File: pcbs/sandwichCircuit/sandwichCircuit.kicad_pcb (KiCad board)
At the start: 2 copper layers, 2 parts, among them J1 Conn_01x19_Pin, U1 ESP32-DevKitC

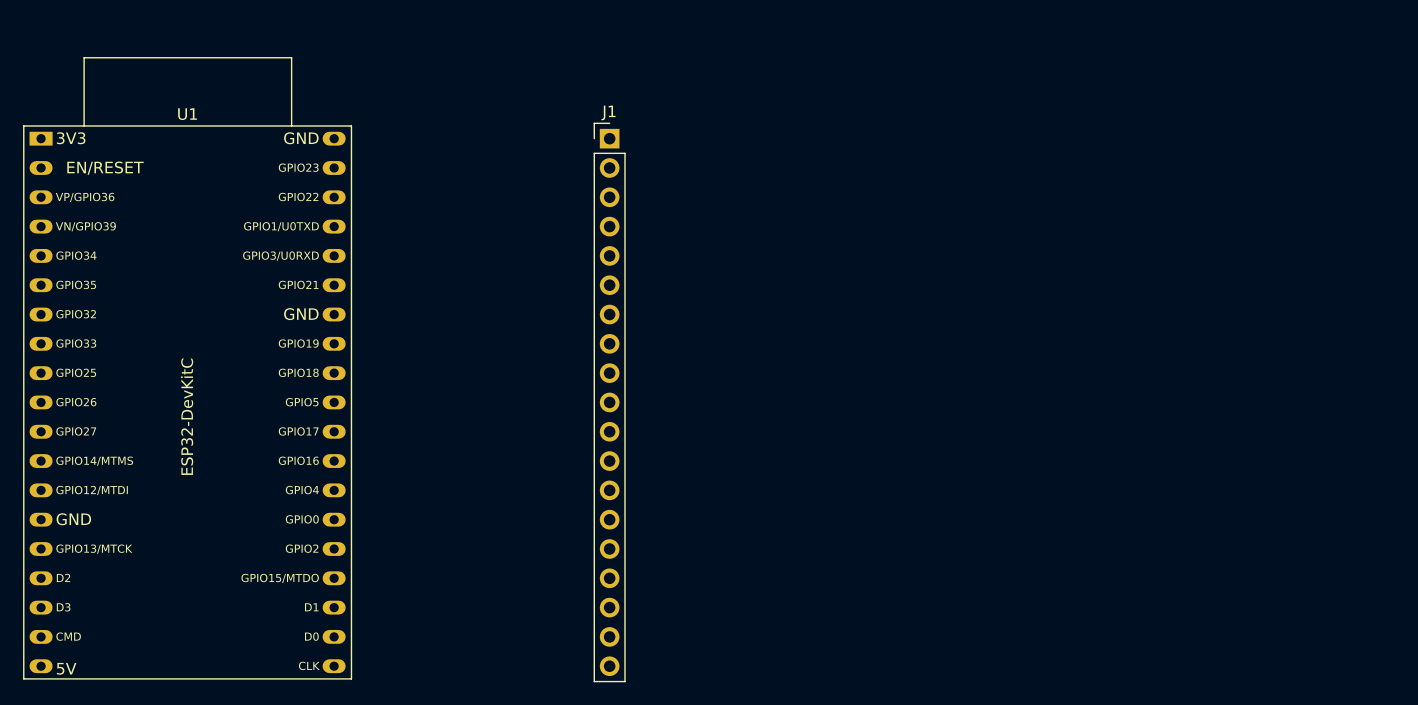
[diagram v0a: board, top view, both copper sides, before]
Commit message: Simplified footprints, schematic revisited
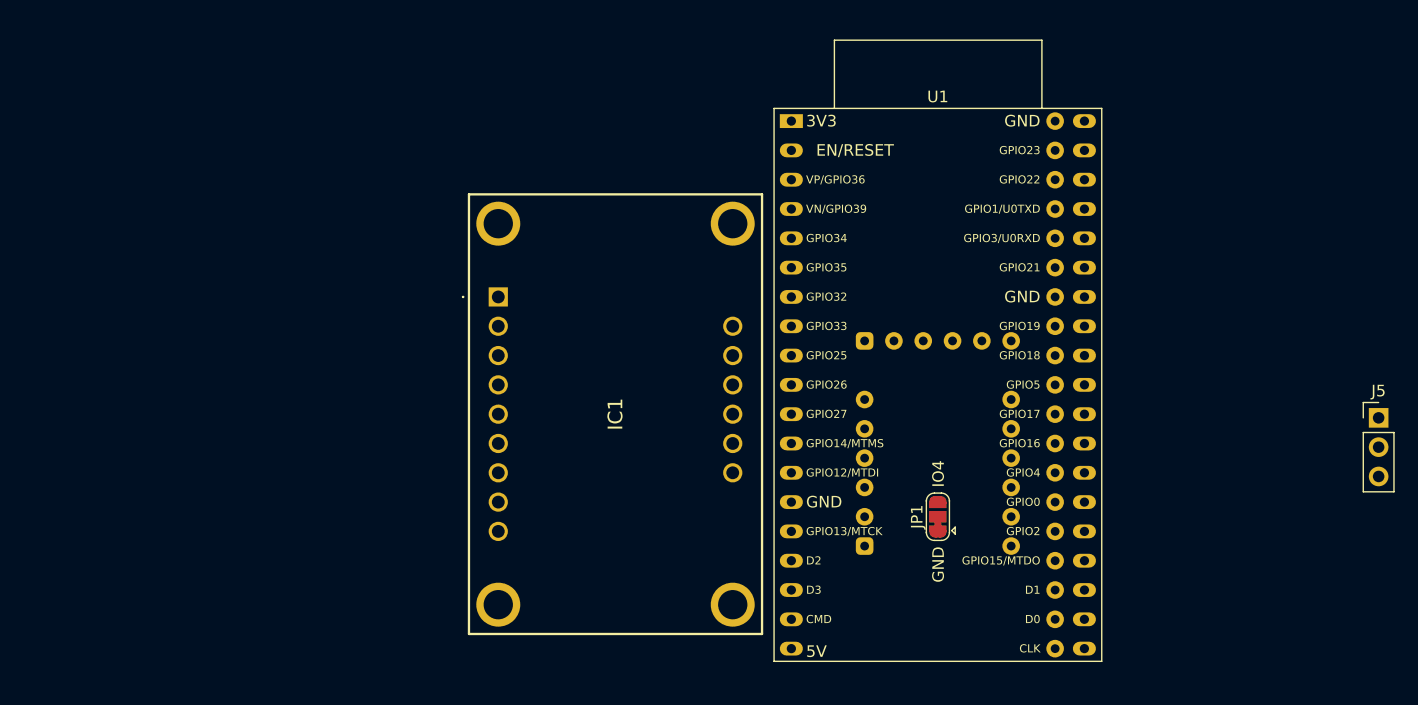
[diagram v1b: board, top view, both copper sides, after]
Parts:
- removed J1: Conn_01x19_Pin, Connector_PinHeader_2.54mm:PinHeader_1x19_P2.54mm_Vertical
- added IC1: 3678, SamacSys_Parts:3678, F.Cu at (127.0, 73.7)
- added J5: Audio Out, Connector_PinHeader_2.54mm:PinHeader_1x03_P2.54mm_Vertical, F.Cu at (203.3, 84.1)
- added JP1: SolderJumper_3_Bridged12, Jumper:SolderJumper-3_P1.3mm_Bridged12_RoundedPad1.0x1.5mm, F.Cu at (165.1, 92.7)
- added U2: CP2104 USB A board, DIY:CP2104_USB_Board, B.Cu at (165.1, 88.9)
- U1: value ESP32-DevKitC -> ESP32-DevKitC header
- moved U1 80.6 mm to (165.1, 81.3)
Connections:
- U1 pad 1: unconnected-(U1-3V3-Pad1) -> +3.3V
- U1 pad 10: unconnected-(U1-DAC_2/ADC2_CH9/GPIO26-Pad10) -> DIN
- U1 pad 11: unconnected-(U1-ADC2_CH7/GPIO27-Pad11) -> BCLK
- U1 pad 19: unconnected-(U1-5V-Pad19) -> +5V
- U1 pad 23: unconnected-(U1-MTDO/GPIO15/ADC2_CH3-Pad23) -> GPIO15
- U1 pad 27: GPIO16 -> GPIO16/U1RXD
- U1 pad 28: GPIO17 -> GPIO17/U1TXD
- U1 pad 9: unconnected-(U1-DAC_1/ADC2_CH8/GPIO25-Pad9) -> GPIO25
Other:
- board text added: "GND"
- board text added: "IO4"

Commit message: v0.1 of simple carrier board
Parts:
- added H1: MountingHole_Pad, MountingHole:MountingHole_3.2mm_M3_Pad_TopBottom, F.Cu at (184.0, 55.0)
- added H2: MountingHole_Pad, MountingHole:MountingHole_3.2mm_M3_Pad_TopBottom, F.Cu at (118.0, 55.0)
- added H3: MountingHole_Pad, MountingHole:MountingHole_3.2mm_M3_Pad_TopBottom, F.Cu at (118.0, 101.0)
- added H4: MountingHole_Pad, MountingHole:MountingHole_3.2mm_M3_Pad_TopBottom, F.Cu at (184.0, 101.0)
- IC1: footprint SamacSys_Parts:3678 -> DIY:Adafruit 3678
- moved J5 85.2 mm to (118.4, 91.4), turned to 180 degrees
- moved IC1 2.87 mm to (126.4, 76.5)
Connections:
- J5 pad 1: AGND -> ROUT
- J5 pad 2: ROUT -> AGND
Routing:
- net +5V: track 0.00 -> 85.4 mm
- net +3.3V: track 0.00 -> 70.6 mm
- net BCLK: track 0.00 -> 37.3 mm
- net DIN: track 0.00 -> 34.3 mm
- net GPIO25: track 0.00 -> 33.1 mm
- net GPIO16/U1RXD: track 0.00 -> 22.4 mm, vias 0 -> 1
- net GPIO17/U1TXD: track 0.00 -> 22.1 mm
- net GPIO4: track 0.00 -> 13.7 mm
- net ROUT: track 0.00 -> 9.68 mm
- net LOUT: track 0.00 -> 9.68 mm
- net AGND: track 0.00 -> 9.68 mm
- net DCD: track 0.00 -> 6.35 mm
- net GPIO5: track 0.00 -> 2.54 mm
- net GPIO3/U0RXD: track 0.00 -> 2.54 mm
- net GPIO23: track 0.00 -> 2.54 mm
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- added copper zone on B.Cu, net GND
- added copper zone on F.Cu, net GND
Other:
- board outline added: 76 x 56 mm
- board text added: "${TITLE} rev${REVISION} - (c) Martin Roger - ${ISSUE_DATE}"
- board text added: "ANTENNA"
- board text added: "G"
- board text added: "L"
- board text added: "R"
- board text added: "USB"

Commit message: Sandwich board 0.1.1
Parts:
- added JP2: SolderJumper_2_Bridged, Jumper:SolderJumper-2_P1.3mm_Bridged_RoundedPad1.0x1.5mm, F.Cu at (181.6, 94.9)
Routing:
- net GPIO15: track 2.54 -> 7.11 mm
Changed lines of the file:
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@@
   (title_block
     (title "Simple carrier board (CP2104)")
-    (date "2025-02-20")
-    (rev "0.1")
+    (date "2025-02-26")
+    (rev "0.1.1")
   )
   (layers
@@
     (pad "MH4" thru_hole circle (at -6.35 -20.32) (size 3.81 3.81) (drill 2.54) (layers "*.Cu" "*.Mask" "F.SilkS")
       (net 1 "unconnected-(IC1-PadMH4)") (pinfunction "MH4") (pintype "passive+no_connect"))
+  )
+  (footprint "Jumper:SolderJumper-2_P1.3mm_Bridged_RoundedPad1.0x1.5mm" (layer "F.Cu")
+    (at 181.61 94.884 90)
+    (descr "SMD Solder Jumper, 1x1.5mm, rounded Pads, 0.3mm gap, bridged with 1 copper strip")
+    (tags "net tie solder jumper bridged")
+    (property "Sheetfile" "sandwichCircuit.kicad_sch")
+    (property "Sheetname" "")
+    (property "ki_description" "Solder Jumper, 2-pole, closed/bridged")
+    (property "ki_keywords" "solder jumper SPST")
+    (attr exclude_from_pos_files)
+    (net_tie_pad_groups "1, 2")
+    (fp_text reference "JP2" (at 2.301 0 180) (layer "F.SilkS")
+        (effects (font (size 1 1) (thickness 0.15)))
+    )
+    (fp_text value "SolderJumper_2_Bridged" (at 0 1.9 90) (layer "F.Fab")
+        (effects (font (size 1 1) (thickness 0.15)))
+    )
+    (fp_poly
+      (pts
+        (xy 0.25 -0.3)
+        (xy -0.25 -0.3)
+        (xy -0.25 0.3)
+        (xy 0.25 0.3)
+      )
+      (stroke (width 0) (type solid)) (fill solid) (layer "F.Cu"))
+    (fp_line (start -1.4 0.3) (end -1.4 -0.3)
+      (stroke (width 0.12) (type solid)) (layer "F.SilkS"))
+    (fp_line (start -0.7 -1) (end 0.7 -1)
+      (stroke (width 0.12) (type solid)) (layer "F.SilkS"))
+    (fp_line (start 0.7 1) (end -0.7 1)
+      (stroke (width 0.12) (type solid)) (layer "F.SilkS"))
+    (fp_line (start 1.4 -0.3) (end 1.4 0.3)
+      (stroke (width 0.12) (type solid)) (layer "F.SilkS"))
+    (fp_arc (start -1.4 -0.3) (mid -1.194975 -0.794975) (end -0.7 -1)
+      (stroke (width 0.12) (type solid)) (layer "F.SilkS"))
+    (fp_arc (start -0.7 1) (mid -1.194975 0.794975) (end -1.4 0.3)
+      (stroke (width 0.12) (type solid)) (layer "F.SilkS"))
+    (fp_arc (start 0.7 -1) (mid 1.194975 -0.794975) (end 1.4 -0.3)
+      (stroke (width 0.12) (type solid)) (layer "F.SilkS"))
+    (fp_arc (start 1.4 0.3) (mid 1.194975 0.794975) (end 0.7 1)
+      (stroke (width 0.12) (type solid)) (layer "F.SilkS"))
+    (fp_line (start -1.65 -1.25) (end -1.65 1.25)
+      (stroke (width 0.05) (type solid)) (layer "F.CrtYd"))
+    (fp_line (start -1.65 -1.25) (end 1.65 -1.25)
+      (stroke (width 0.05) (type solid)) (layer "F.CrtYd"))
+    (fp_line (start 1.65 1.25) (end -1.65 1.25)
+      (stroke (width 0.05) (type solid)) (layer "F.CrtYd"))
+    (fp_line (start 1.65 1.25) (end 1.65 -1.25)
+      (stroke (width 0.05) (type solid)) (layer "F.CrtYd"))
+    (pad "1" smd custom (at -0.65 0 90) (size 1 0.5) (layers "F.Cu" "F.Mask")
+      (net 34 "GPIO15") (pinfunction "A") (pintype "passive") (zone_connect 2) (thermal_bridge_angle 45)
+      (options (clearance outline) (anchor rect))
+      (primitives
+        (gr_circle (center 0 0.25) (end 0.5 0.25) (width 0) (fill yes))
+        (gr_circle (center 0 -0.25) (end 0.5 -0.25) (width 0) (fill yes))
+        (gr_poly
+          (pts
+            (xy 0.5 0.75)
+            (xy 0 0.75)
+            (xy 0 -0.75)
+            (xy 0.5 -0.75)
+          )
+          (width 0) (fill yes))
+      ))
+    (pad "2" smd custom (at 0.65 0 90) (size 1 0.5) (layers "F.Cu" "F.Mask")
+      (net 20 "GND") (pinfunction "B") (pintype "passive") (zone_connect 2) (thermal_bridge_angle 45)
+      (options (clearance outline) (anchor rect))
+      (primitives
+        (gr_circle (center 0 0.25) (end 0.5 0.25) (width 0) (fill yes))
+        (gr_circle (center 0 -0.25) (end 0.5 -0.25) (width 0) (fill yes))
+        (gr_poly
+          (pts
+            (xy 0 0.75)
+            (xy -0.5 0.75)
+            (xy -0.5 -0.75)
+            (xy 0 -0.75)
+          )
+          (width 0) (fill yes))
+      ))
   )
   (footprint "MountingHole:MountingHole_3.2mm_M3_Pad_TopBottom" (layer "F.Cu")
@@
   (segment (start 175.26 91.44) (end 177.8 91.44) (width 0.1524) (layer "F.Cu") (net 32))
   (segment (start 175.26 93.98) (end 177.8 93.98) (width 0.1524) (layer "F.Cu") (net 33))
+  (segment (start 181.61 96.139) (end 181.61 95.534) (width 0.254) (layer "F.Cu") (net 34))
+  (segment (start 177.8 96.52) (end 181.229 96.52) (width 0.254) (layer "F.Cu") (net 34))
+  (segment (start 181.229 96.52) (end 181.61 96.139) (width 0.254) (layer "F.Cu") (net 34))
   (segment (start 175.26 96.52) (end 177.8 96.52) (width 0.1524) (layer "F.Cu") (net 34))
   (segment (start 175.26 99.06) (end 177.8 99.06) (width 0.1524) (layer "F.Cu") (net 35))

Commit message: Sandwich board adjustments
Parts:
- JP1: moved to B.Cu
- moved JP1 16.5 mm to (181.6, 92.7)
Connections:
- JP1 pad 3: GPIO4 -> GPIO5
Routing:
- net GPIO5: track 2.54 -> 15.8 mm
- net GPIO4: track 13.7 -> 2.54 mm
- net DCD: track 6.35 -> 10.1 mm
- net GND: vias 309 -> 313
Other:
- board text added: "DCD"
- board text added: "IO15"
- board text added: "IO5"

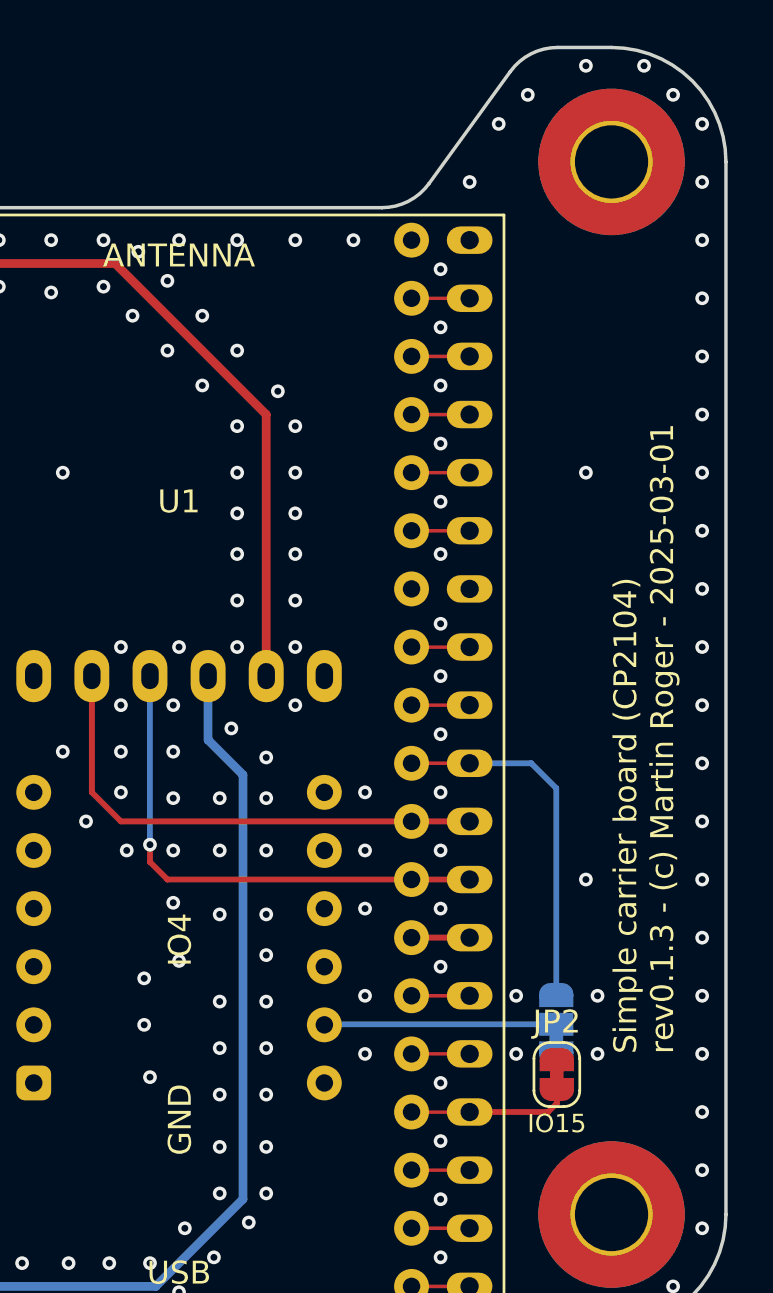
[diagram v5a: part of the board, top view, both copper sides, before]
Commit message: Sandwich board correction
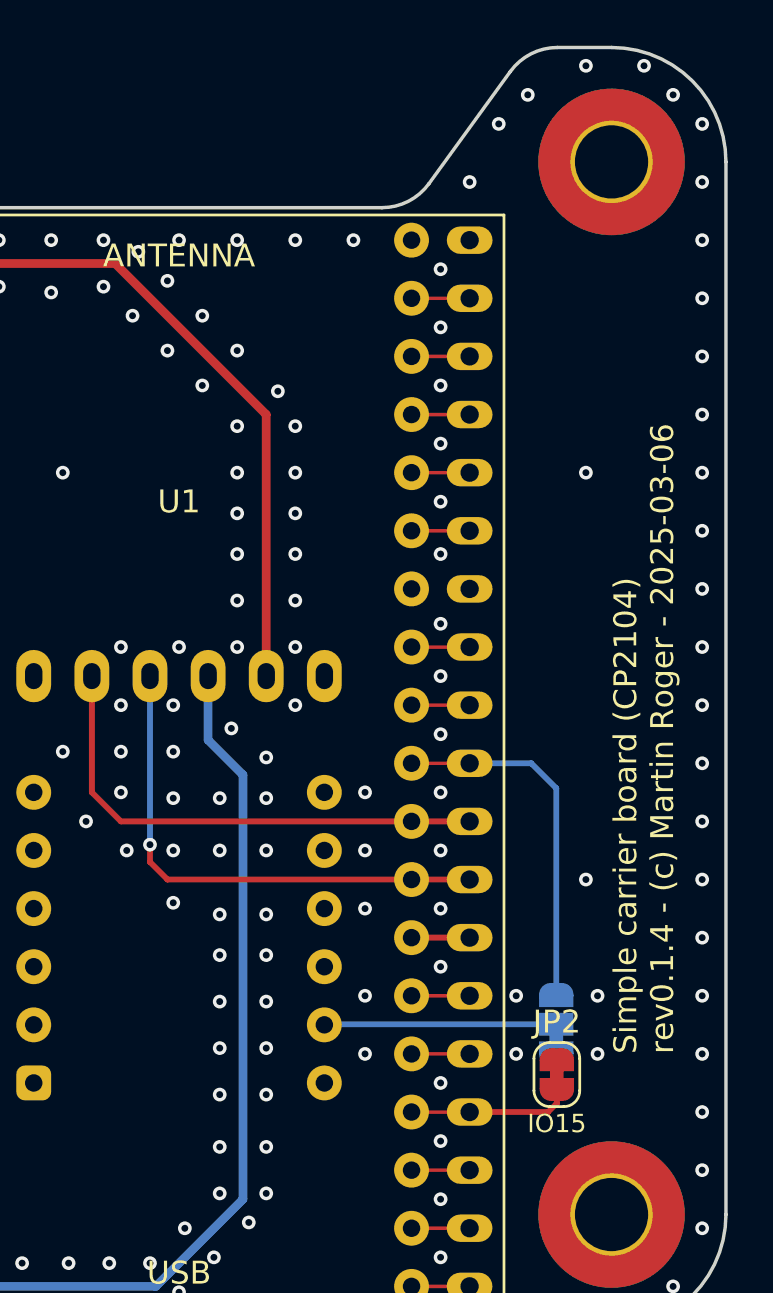
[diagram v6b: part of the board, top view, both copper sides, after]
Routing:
- net GND: vias 313 -> 310
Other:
- board text removed: "GND"
- board text removed: "IO4"
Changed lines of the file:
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@@
   (title_block
     (title "Simple carrier board (CP2104)")
-    (date "2025-03-01")
-    (rev "0.1.3")
+    (date "2025-03-06")
+    (rev "0.1.4")
     (company "Martin Roger")
   )
@@
     (effects (font (size 1 1) (thickness 0.15)) (justify left))
   )
-  (gr_text "IO4" (at 165.735 90.17 90) (layer "F.SilkS")
-    (effects (font (size 1 1) (thickness 0.15)) (justify left bottom))
-  )
   (gr_text "G" (at 116.332 88.9 90) (layer "F.SilkS")
     (effects (font (size 1 1) (thickness 0.15)) (justify bottom))
-  )
-  (gr_text "GND" (at 165.735 98.425 90) (layer "F.SilkS")
-    (effects (font (size 1 1) (thickness 0.15)) (justify left bottom))
   )
   (gr_text "ANTENNA" (at 165.1 59.69) (layer "F.SilkS")
@@
   (via (at 135.128 77.978) (size 0.6) (drill 0.3) (layers "F.Cu" "B.Cu") (free) (net 20))
   (via (at 167.64 58.42) (size 0.6) (drill 0.3) (layers "F.Cu" "B.Cu") (free) (net 20))
-  (via (at 163.83 94.996) (size 0.6) (drill 0.3) (layers "F.Cu" "B.Cu") (free) (net 20))
   (via (at 152.146 59.69) (size 0.6) (drill 0.3) (layers "F.Cu" "B.Cu") (free) (net 20))
   (via (at 159.512 60.706) (size 0.6) (drill 0.3) (layers "F.Cu" "B.Cu") (free) (net 20))
@@
   (via (at 149.86 75.692) (size 0.6) (drill 0.3) (layers "F.Cu" "B.Cu") (free) (net 20))
   (via (at 164.846 80.772) (size 0.6) (drill 0.3) (layers "F.Cu" "B.Cu") (free) (net 20))
-  (via (at 163.576 90.678) (size 0.6) (drill 0.3) (layers "F.Cu" "B.Cu") (free) (net 20))
   (via (at 137.922 62.738) (size 0.6) (drill 0.3) (layers "F.Cu" "B.Cu") (free) (net 20))
   (via (at 134.874 84.074) (size 0.6) (drill 0.3) (layers "F.Cu" "B.Cu") (free) (net 20))
@@
   (via (at 176.53 87.63) (size 0.6) (drill 0.3) (layers "F.Cu" "B.Cu") (free) (net 20))
   (via (at 136.652 76.454) (size 0.6) (drill 0.3) (layers "F.Cu" "B.Cu") (free) (net 20))
-  (via (at 163.576 92.71) (size 0.6) (drill 0.3) (layers "F.Cu" "B.Cu") (free) (net 20))
   (via (at 120.142 92.71) (size 0.6) (drill 0.3) (layers "F.Cu" "B.Cu") (free) (net 20))
   (via (at 132.08 50.8) (size 0.6) (drill 0.3) (layers "F.Cu" "B.Cu") (free) (net 20))
@@
   (via (at 141.986 61.468) (size 0.6) (drill 0.3) (layers "F.Cu" "B.Cu") (free) (net 20))
   (via (at 187.96 66.04) (size 0.6) (drill 0.3) (layers "F.Cu" "B.Cu") (free) (net 20))
-  (via (at 165.1 89.916) (size 0.6) (drill 0.3) (layers "F.Cu" "B.Cu") (free) (net 20))
+  (via (at 166.878 89.662) (size 0.6) (drill 0.3) (layers "F.Cu" "B.Cu") (free) (net 20))
   (via (at 166.878 100.076) (size 0.6) (drill 0.3) (layers "F.Cu" "B.Cu") (free) (net 20))
   (via (at 139.954 70.104) (size 0.6) (drill 0.3) (layers "F.Cu" "B.Cu") (free) (net 20))
